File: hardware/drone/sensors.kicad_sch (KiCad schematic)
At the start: 4 parts, among them U14 ICM-42688-P

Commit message: Finished GNSS, did more pinmuxxing
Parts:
- added C49, C55: 100n, symbol Device:C
- added U15: SAM_M10Q, Package_LGA:LGA-16_3x3mm_P0.5mm_LayoutBorder3x5y, symbol SoftDrone:SAM_M10Q
- added U17: TXU0204, symbol SoftDrone:TXU0204
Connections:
- net GND: now also C49.2, C55.2, U15.1 (GND), U15.10 (GND), U15.11 (GND), U15.15 (GND), U15.16 (GND), U15.20 (GND), U15.4 (GND), U15.5 (GND), U15.6 (GND), U17.7 (GND)
- net VDD1V8: now also C49.1, U17.1 (VCCA), U17.8 (OE)
- new net GNSS_RESET_N_1V8: U17.3 (A2)
- new net GNSS_RESET_N_3V3: U15.18 (RESET_N), U17.12 (B2Y)
- new net GNSS_TIM_1V8: U17.5 (A4Y)
- new net GNSS_TIM_3V3: U15.7 (TIMEPULSE), U17.10 (B4)
- new net GNSS_UART4_RX_1V8: U17.2 (A1)
- new net GNSS_UART4_RX_3V3: U15.14 (RXD), U17.11 (B3)
- new net GNSS_UART4_TX_1V8: U17.4 (A3Y)
- new net GNSS_UART4_TX_3V3: U15.13 (TXD), U17.13 (B1Y)
- new net VDD3V3: C55.1, U15.17 (VCC), U15.2 (V_IO), U17.14 (VCCB)
- no-connect marks 0 -> 5
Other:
- note added: "GNSS"
- note added: "IMU"
- note added: "Levelshifting"
- moved on the sheet: C82, C83, C84, U14

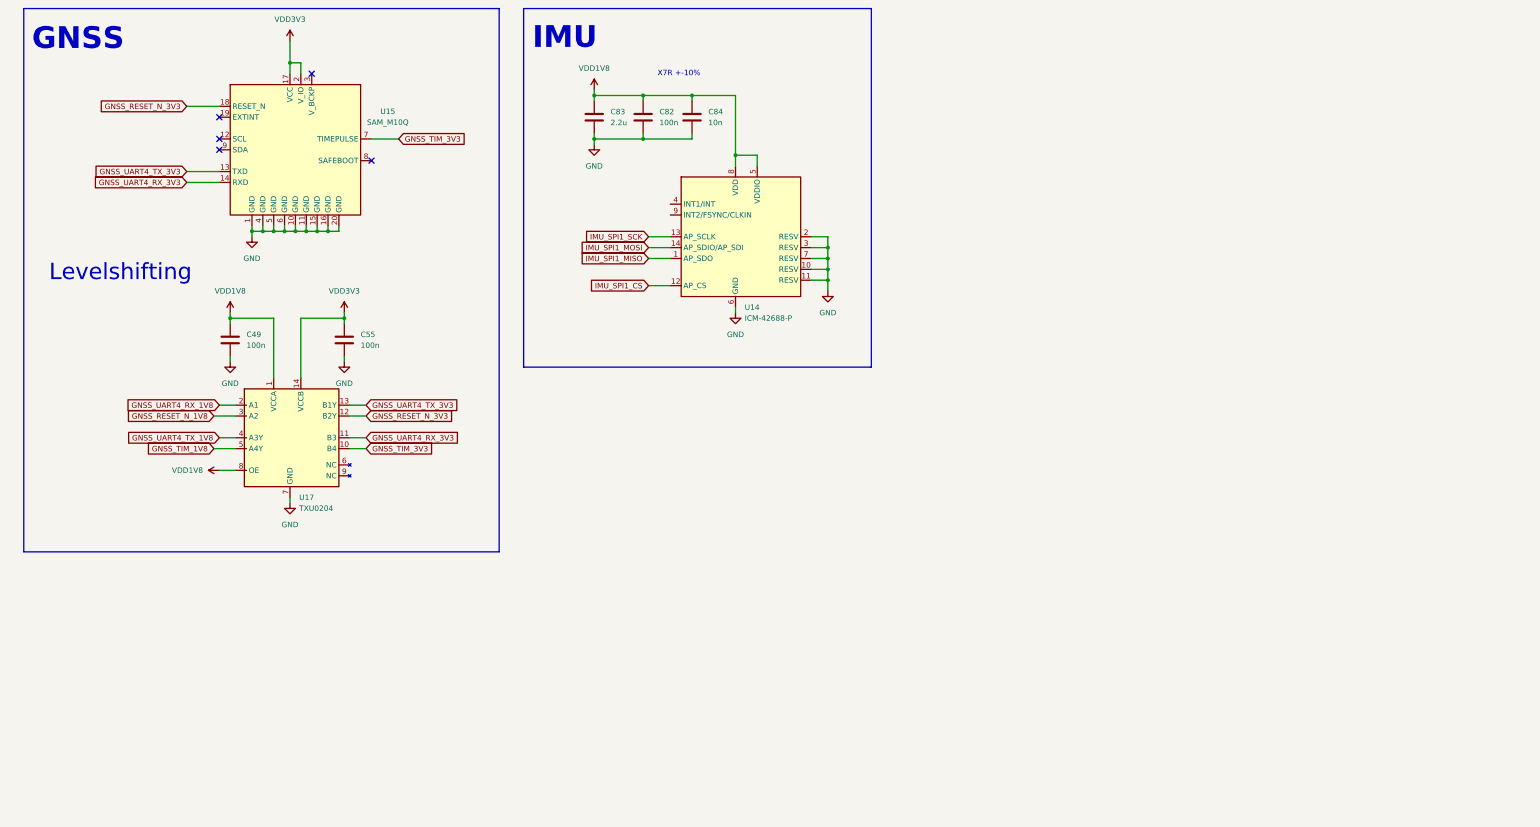
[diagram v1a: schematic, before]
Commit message: Added barometer, more pinmuxxing, added VBAT sensing and reverse voltage protection
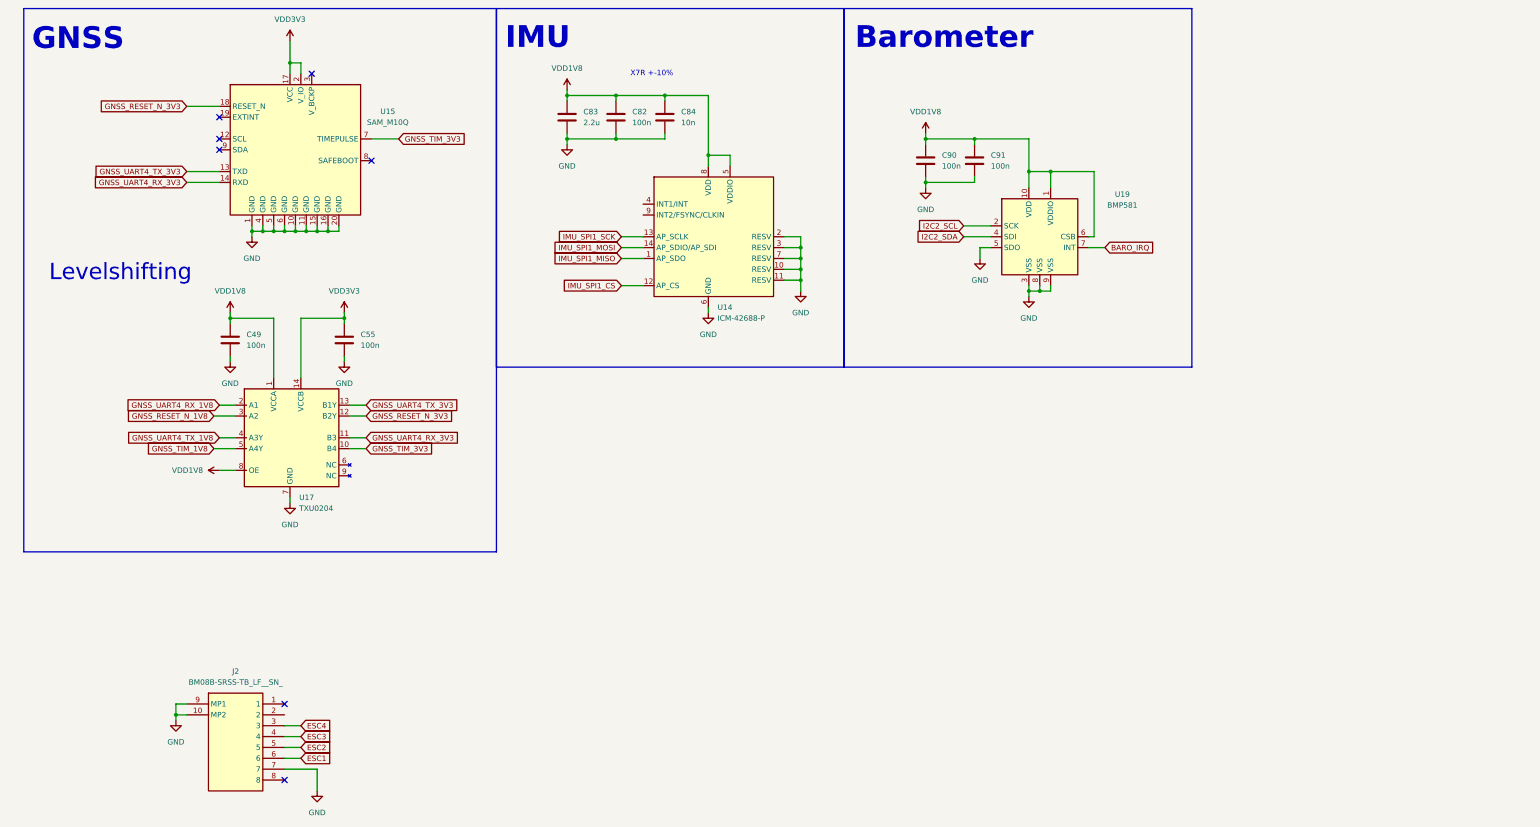
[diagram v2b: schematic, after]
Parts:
- added C90, C91: 100n, symbol Device:C
- added J2: BM08B-SRSS-TB_LF__SN_, BM08BSRSSTBLFSN, symbol BM08B-SRSS-TB_LF__SN_:BM08B-SRSS-TB_LF__SN_
- added U19: BMP581, symbol SoftDrone:BMP581
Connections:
- net GND: now also C90.2, C91.2, J2.10 (MP2), J2.7, J2.9 (MP1), U19.3 (VSS), U19.5 (SDO), U19.8 (VSS), U19.9 (VSS)
- net VDD1V8: now also C90.1, C91.1, U19.1 (VDDIO), U19.10 (VDD), U19.6 (CSB)
- new net BARO_IRQ: U19.7 (INT)
- new net ESC1: J2.6
- new net ESC2: J2.5
- new net ESC3: J2.4
- new net ESC4: J2.3
- new net I2C2_SCL: U19.2 (SCK)
- new net I2C2_SDA: U19.4 (SDI)
- no-connect marks 5 -> 7
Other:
- note added: "Barometer"
- moved on the sheet: C82, C83, C84, U14

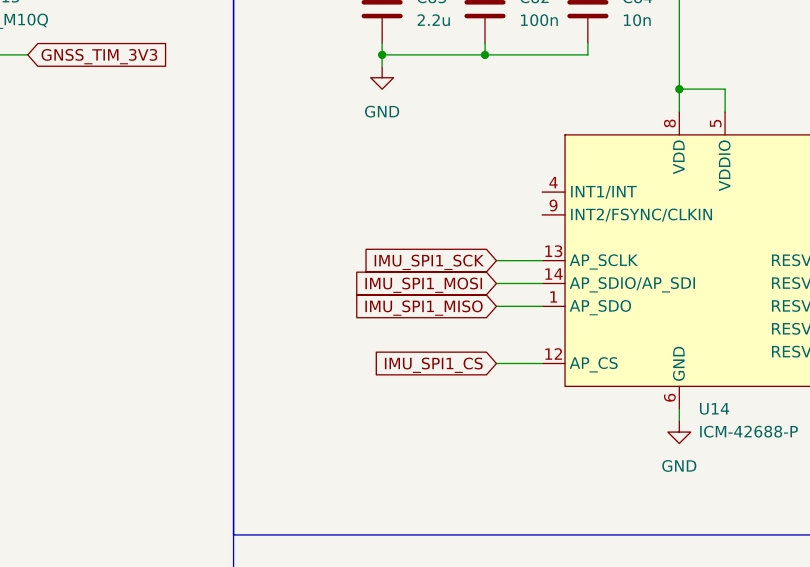
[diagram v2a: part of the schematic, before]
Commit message: Finished MCU schematic decoupling, finished system control schematic
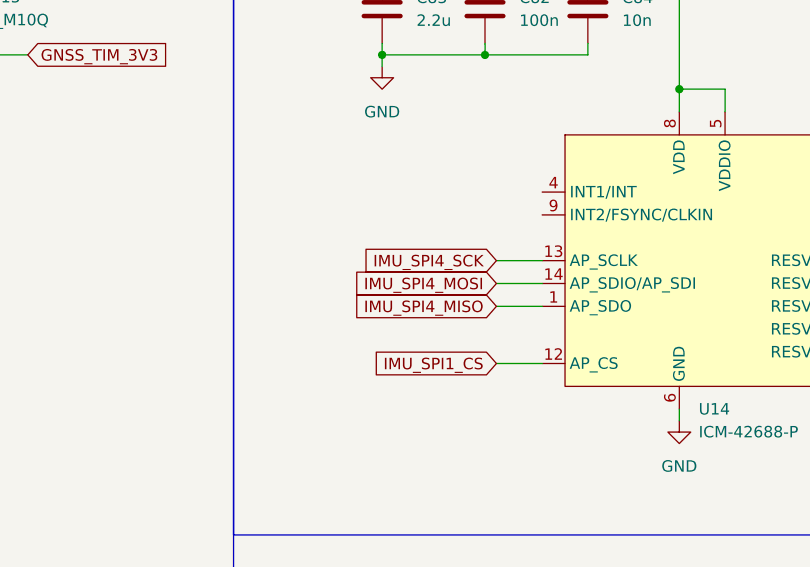
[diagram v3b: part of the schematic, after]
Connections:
- net IMU_SPI1_MISO renamed IMU_SPI4_MISO
- net IMU_SPI1_MOSI renamed IMU_SPI4_MOSI
- net IMU_SPI1_SCK renamed IMU_SPI4_SCK
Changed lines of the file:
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@@
 		)
 	)
-	(global_label "IMU_SPI1_MISO"
+	(global_label "IMU_SPI4_MISO"
 		(shape input)
 		(at 163.83 101.6 180)
@@
 		)
 	)
-	(global_label "IMU_SPI1_MOSI"
+	(global_label "IMU_SPI4_MOSI"
 		(shape input)
 		(at 163.83 99.06 180)
@@
 		)
 	)
-	(global_label "IMU_SPI1_SCK"
+	(global_label "IMU_SPI4_SCK"
 		(shape input)
 		(at 163.83 96.52 180)

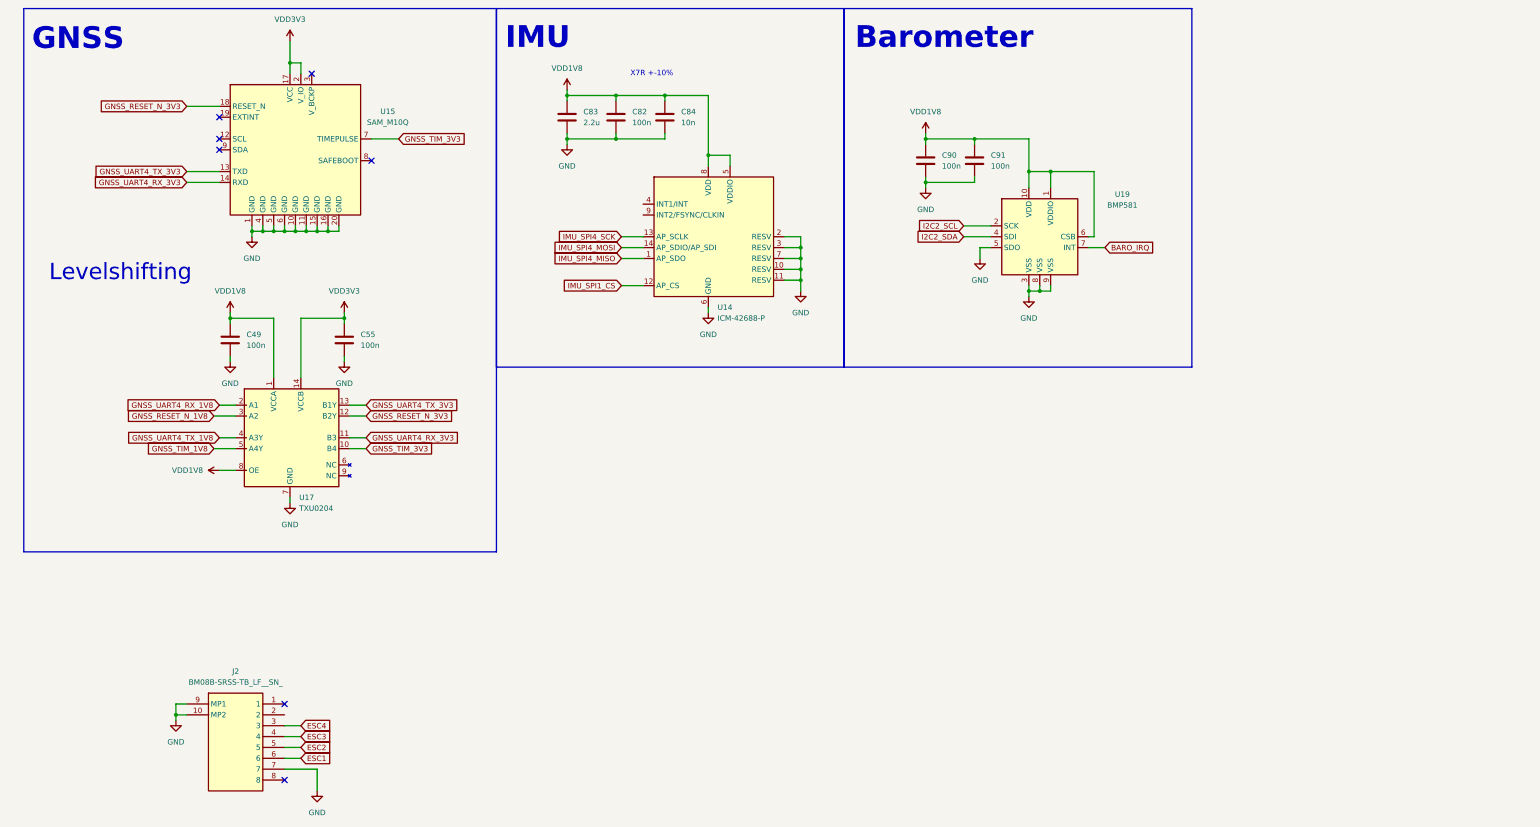
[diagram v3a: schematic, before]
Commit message: Added magnetometer
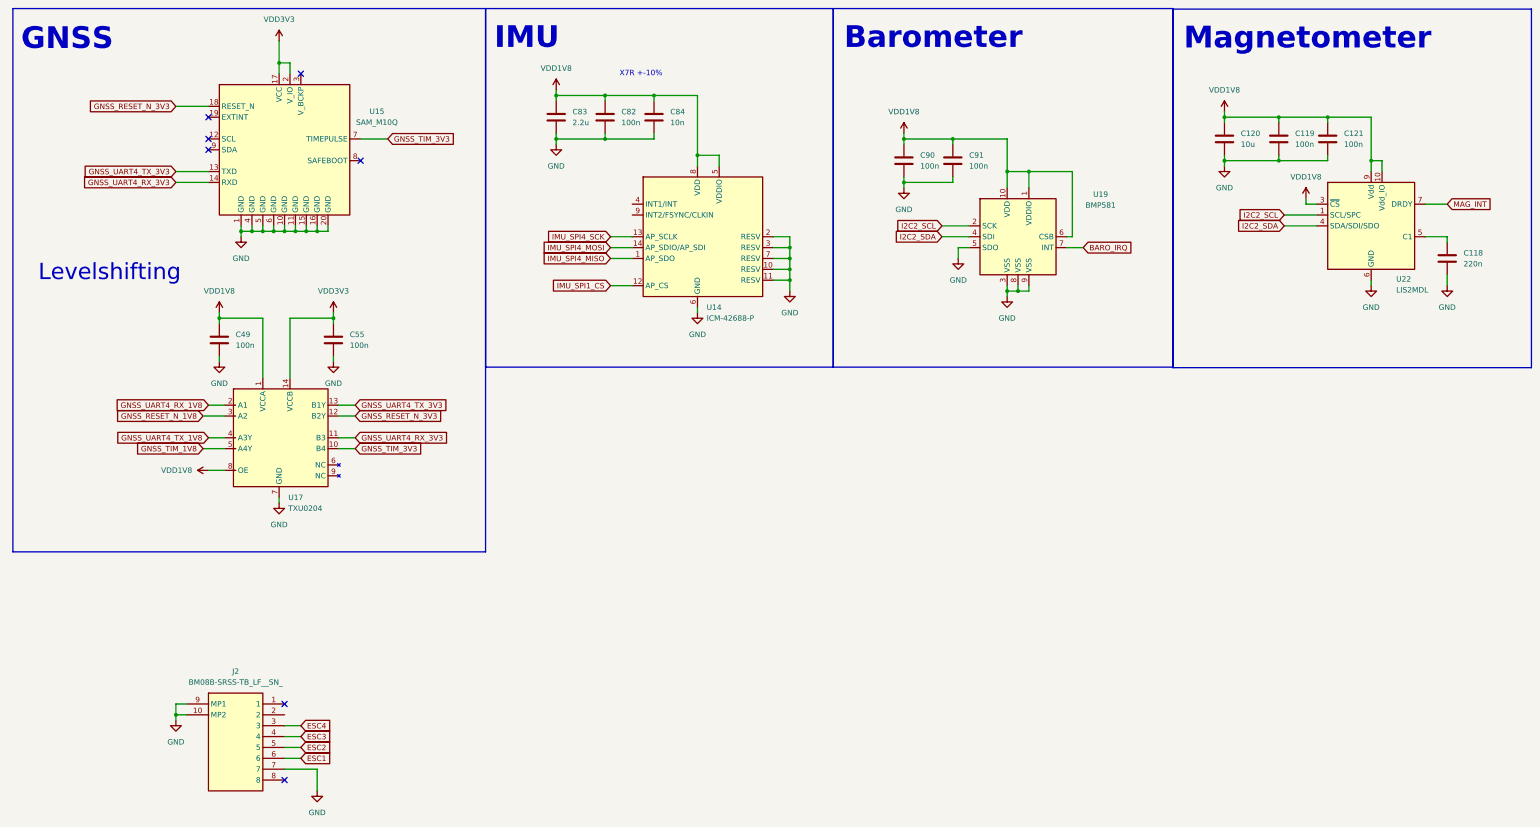
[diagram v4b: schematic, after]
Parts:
- added C118: 220n, Package_LGA:LGA-12_2x2mm_P0.5mm, symbol Device:C
- added C119, C121: 100n, symbol Device:C
- added C120: 10u, symbol Device:C
- added U22: LIS2MDL, Package_LGA:LGA-12_2x2mm_P0.5mm, symbol Sensor_Magnetic:LIS2MDL
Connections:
- net GND: now also C118.2, C119.2, C120.2, C121.2, U22.6 (GND), U22.8 (GND)
- net I2C2_SCL: now also U22.1 (SCL/SPC)
- net I2C2_SDA: now also U22.4 (SDA/SDI/SDO)
- net VDD1V8: now also C119.1, C120.1, C121.1, U22.10 (Vdd_IO), U22.3 (~{CS}), U22.9 (Vdd)
- new net: C118.1, U22.5 (C1)
- new net MAG_INT: U22.7 (DRDY)
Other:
- note added: "Magnetometer"
- moved on the sheet: C49, C55, C82, C83, C84, C90, C91, U14, U15, U17, U19

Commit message: Small cleanup
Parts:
- J2: footprint BM08BSRSSTBLFSN -> (none)
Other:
- note added: "Need to figure out voltage requirement for esc board"
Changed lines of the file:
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@@
 		)
 	)
+	(text "Need to figure out voltage requirement for esc board"
+		(exclude_from_sim no)
+		(at 113.03 195.58 0)
+		(effects
+			(font
+				(size 1.27 1.27)
+			)
+		)
+	)
 	(text "IMU"
 		(exclude_from_sim no)
@@
 			)
 		)
-		(property "Footprint" "BM08BSRSSTBLFSN"
+		(property "Footprint" ""
 			(at 81.28 300.66 0)
 			(hide yes)

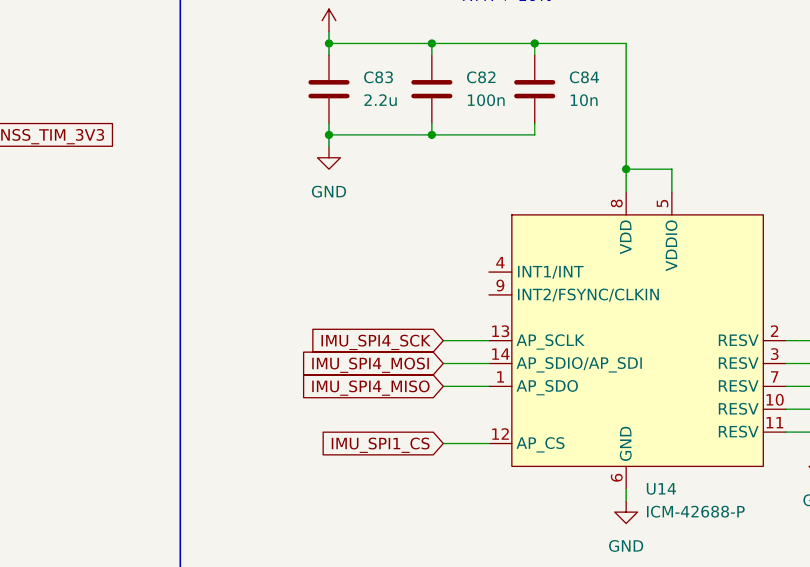
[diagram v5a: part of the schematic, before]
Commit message: Fixed some pullups and pinmuxxed more
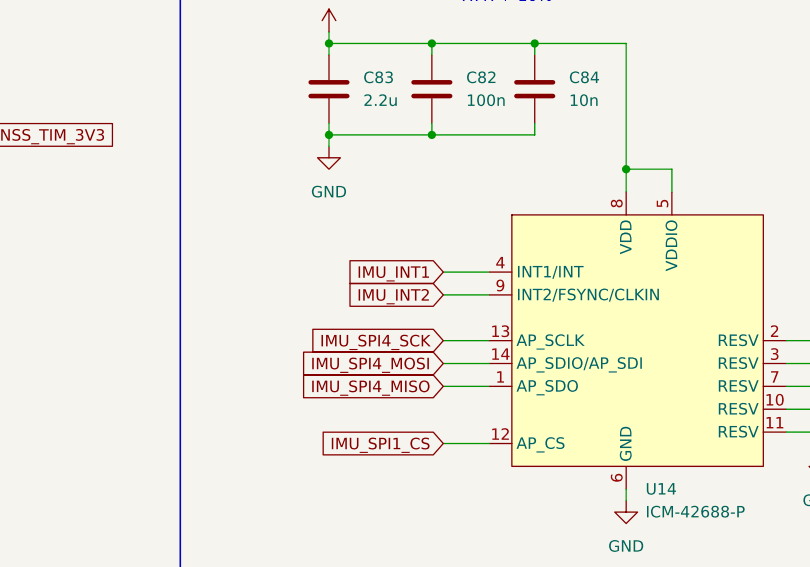
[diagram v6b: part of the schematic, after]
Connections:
- net IMU_INT1: now reaches U14.4 (INT1/INT)
- net IMU_INT2: now reaches U14.9 (INT2/FSYNC/CLKIN)
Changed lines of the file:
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@@
+	(wire
+		(pts
+			(xy 161.29 88.9) (xy 166.37 88.9)
+		)
+		(stroke
+			(width 0)
+			(type default)
+		)
+	)
 	(wire
 		(pts
@@
 	(wire
 		(pts
+			(xy 161.29 91.44) (xy 166.37 91.44)
+		)
+		(stroke
+			(width 0)
+			(type default)
+		)
+	)
+	(wire
+		(pts
 			(xy 83.82 55.88) (xy 83.82 58.42)
 		)
@@
 		)
 	)
+	(global_label "IMU_INT1"
+		(shape input)
+		(at 161.29 88.9 180)
+		(fields_autoplaced yes)
+		(effects
+			(font
+				(size 1.27 1.27)
+			)
+			(justify right)
+		)
+		(property "Intersheetrefs" "${INTERSHEET_REFS}"
+			(at 149.8381 88.9 0)
+			(hide yes)
+			(show_name no)
+			(do_not_autoplace no)
+			(effects
+				(font
+					(size 1.27 1.27)
+				)
+				(justify right)
+			)
+		)
+	)
 	(global_label "GNSS_TIM_3V3"
 		(shape input)
@@
 			)
 		)
+	)
+	(global_label "IMU_INT2"
+		(shape input)
+		(at 161.29 91.44 180)
+		(fields_autoplaced yes)
+		(effects
+			(font
+				(size 1.27 1.27)
+			)
+			(justify right)
+		)
+		(property "Intersheetrefs" "${INTERSHEET_REFS}"
+			(at 149.8381 91.44 0)
+			(hide yes)
+			(show_name no)
+			(do_not_autoplace no)
+			(effects
+				(font
+					(size 1.27 1.27)
+				)
+				(justify right)
+			)
+		)

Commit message: Finished power budget - worst case table
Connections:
- net ESC1: now also J2.3; no longer J2.6
- net ESC2: now also J2.4; no longer J2.5
- net ESC3: now also J2.5; no longer J2.4
- net ESC4: now also J2.6; no longer J2.3
- net GND: now also J2.1; no longer J2.7
- net VBAT_UNPROT: now reaches J2.2

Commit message: Started footprint assignments
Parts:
- C118: footprint Package_LGA:LGA-12_2x2mm_P0.5mm -> (none)
- J2: footprint (none) -> BM08B-SRSS-TB_LF__SN_:BM08BSRSSTBLFSN
- U14, U15: footprint Package_LGA:LGA-16_3x3mm_P0.5mm_LayoutBorder3x5y -> (none)
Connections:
- net VBAT_UNPROT: no longer names the net of J2.2
- no-connect marks 7 -> 8
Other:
- note removed: "Need to figure out voltage requirement for esc board"
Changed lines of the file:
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@@
 		)
 	)
-	(text "Need to figure out voltage requirement for esc board"
-		(exclude_from_sim no)
-		(at 138.176 180.086 0)
-		(effects
-			(font
-				(size 1.27 1.27)
-			)
-		)
-	)
 	(text "IMU"
 		(exclude_from_sim no)
@@
 	)
 	(no_connect
+		(at 85.09 208.28)
+	)
+	(no_connect
 		(at 85.09 223.52)
 	)
@@
 	(wire
 		(pts
-			(xy 101.6 208.28) (xy 85.09 208.28)
-		)
-		(stroke
-			(width 0)
-			(type default)
-		)
-	)
-	(wire
-		(pts
 			(xy 96.52 124.46) (xy 96.52 125.73)
 		)
@@
 	(wire
 		(pts
-			(xy 101.6 207.01) (xy 101.6 208.28)
-		)
-		(stroke
-			(width 0)
-			(type default)
-		)
-	)
-	(wire
-		(pts
 			(xy 254 109.22) (xy 254 110.49)
 		)
@@
 			)
 		)
-		(property "Footprint" "Package_LGA:LGA-16_3x3mm_P0.5mm_LayoutBorder3x5y"
+		(property "Footprint" ""
 			(at 85.09 76.2 0)
 			(hide yes)
@@
 			)
 		)
-		(property "Footprint" ""
+		(property "Footprint" "BM08B-SRSS-TB_LF__SN_:BM08BSRSSTBLFSN"
 			(at 81.28 300.66 0)
 			(hide yes)
@@
 	)
 	(symbol
-		(lib_id "power:VDD")
-		(at 101.6 207.01 0)
-		(unit 1)
-		(body_style 1)
-		(exclude_from_sim no)
-		(in_bom yes)
-		(on_board yes)
-		(in_pos_files yes)
-		(dnp no)
-		(fields_autoplaced yes)
-		(property "Reference" "#PWR0217"
-			(at 101.6 210.82 0)
-			(hide yes)
-			(show_name no)
-			(do_not_autoplace no)
-			(effects
-				(font
-					(size 1.27 1.27)
-				)
-			)
-		)
-		(property "Value" "VBAT_UNPROT"
-			(at 101.6 201.93 0)
-			(show_name no)
-			(do_not_autoplace no)
-			(effects
-				(font
-					(size 1.27 1.27)
-				)
-			)
-		)
-		(property "Footprint" ""
-			(at 101.6 207.01 0)
-			(hide yes)
-			(show_name no)
-			(do_not_autoplace no)
-			(effects
-				(font
-					(size 1.27 1.27)
-				)
-			)
-		)
-		(property "Datasheet" ""
-			(at 101.6 207.01 0)
-			(hide yes)
-			(show_name no)
-			(do_not_autoplace no)
-			(effects
-				(font
-					(size 1.27 1.27)
-				)
-			)
-		)
-		(property "Description" "Power symbol creates a global label with name \"VDD\""
-			(at 101.6 207.01 0)
-			(hide yes)
-			(show_name no)
-			(do_not_autoplace no)
-			(effects
-				(font
-					(size 1.27 1.27)
-				)
-			)
-		)
-		(pin "1"
-		)
-		(instances
-			(project "drone"
-				(path "/62c402a6-ed3f-446b-8423-821e9cc6908b/73325d99-70a4-4158-9179-bdcff983b262"
-					(reference "#PWR0217")
-					(unit 1)
-				)
-			)
-		)
-	)
-	(symbol
 		(lib_id "power:GND")
 		(at 96.52 125.73 0)
@@
 			)
 		)
-		(property "Footprint" "Package_LGA:LGA-12_2x2mm_P0.5mm"
+		(property "Footprint" ""
 			(at 357.8352 105.41 0)
 			(hide yes)
@@
 			)
 		)
-		(property "Footprint" "Package_LGA:LGA-16_3x3mm_P0.5mm_LayoutBorder3x5y"
+		(property "Footprint" ""
 			(at 182.88 95.25 0)
 			(hide yes)
